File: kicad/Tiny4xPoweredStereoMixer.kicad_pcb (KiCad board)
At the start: 4 copper layers, 84 x 67.2 mm, 62 parts, among them J1 AudioJack3_SwitchTR, J2 AudioJack3_SwitchTR, J3 AudioJack3_SwitchTR, J4 AudioJack3_SwitchTR, J5 PowerConnector, J9 AudioJack3_SwitchTR, U1 TL072, U2 TL072, U3 TPS54202DDC

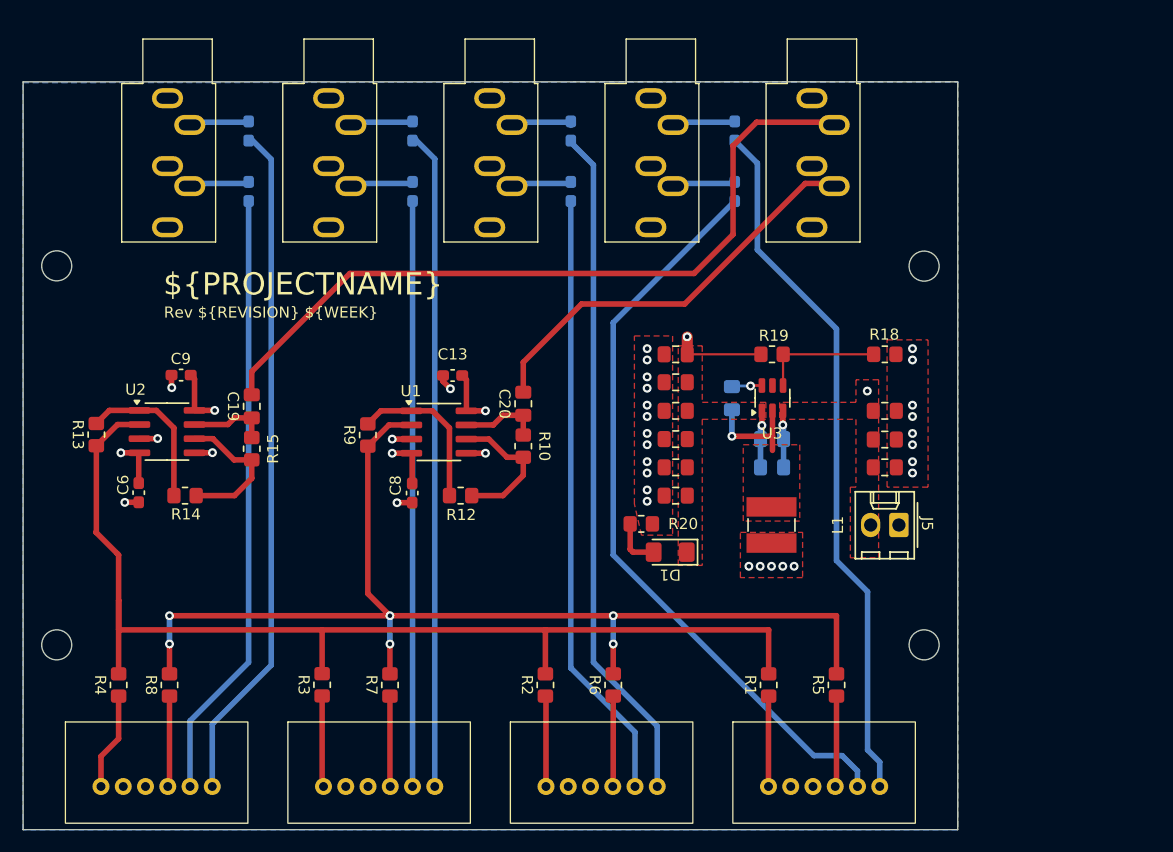
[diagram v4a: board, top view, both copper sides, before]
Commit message: PSU now uses +/- 2.5V; Added barrel jack; updated layout
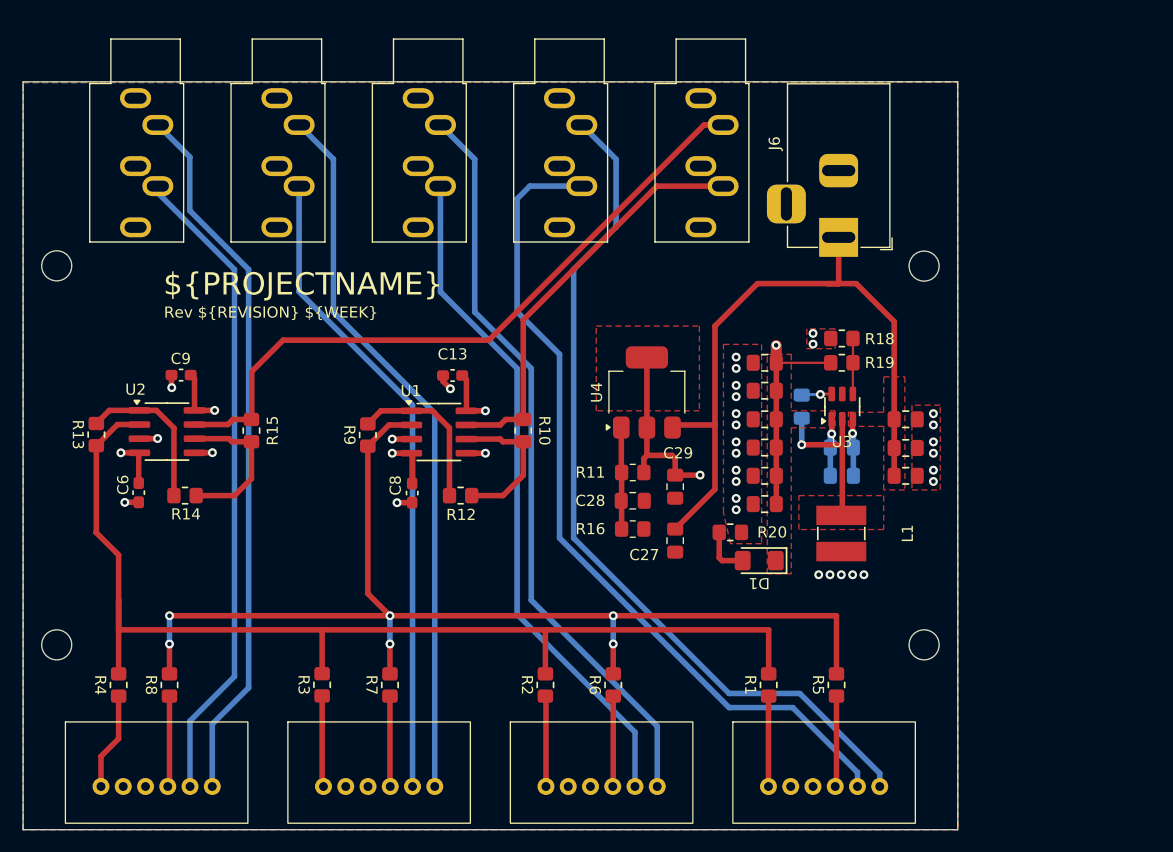
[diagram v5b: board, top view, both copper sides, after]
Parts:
- removed C10, C11, C12, C14, C17, C18, C5, C7: 100nF, Capacitor_SMD:C_0603_1608Metric_Pad1.08x0.95mm_HandSolder
- removed C19, C20: 10uF, Capacitor_SMD:C_0805_2012Metric_Pad1.18x1.45mm_HandSolder
- removed J5: PowerConnector, Connector_Molex:Molex_KK-254_AE-6410-02A_1x02_P2.54mm_Vertical
- added C27: 10uF, Capacitor_SMD:C_0805_2012Metric_Pad1.18x1.45mm_HandSolder, F.Cu at (160.3, 91.7)
- added C28: 22uF, Capacitor_SMD:C_0805_2012Metric_Pad1.18x1.45mm_HandSolder, F.Cu at (156.4, 88.1)
- added C29: 10uF, Capacitor_SMD:C_0805_2012Metric_Pad1.18x1.45mm_HandSolder, F.Cu at (160.3, 86.8)
- added J6: Barrel_Jack_Switch, Connector_BarrelJack:BarrelJack_Horizontal, F.Cu at (174.9, 64.4)
- added R11: 120R, Resistor_SMD:R_0805_2012Metric_Pad1.20x1.40mm_HandSolder, F.Cu at (156.4, 85.6)
- added R16: 120R, Resistor_SMD:R_0805_2012Metric_Pad1.20x1.40mm_HandSolder, F.Cu at (156.4, 90.6)
- added U4: LM1117MP-ADJ, Package_TO_SOT_SMD:SOT-223-3_TabPin2, F.Cu at (157.7, 78.4)
- moved J9 9.98 mm to (162.6, 51.9)
- moved J4 8.21 mm to (149.9, 51.9)
- moved C21 8.04 mm to (168.3, 85.9)
- moved C22 8.04 mm to (168.3, 88.4)
- moved C23 8.04 mm to (168.3, 75.7)
- moved C24 8.04 mm to (168.3, 78.2)
- moved C25 8.04 mm to (168.3, 80.8)
- moved C26 8.04 mm to (168.3, 83.3)
- moved D1 8.04 mm to (167.8, 93.5)
- moved R20 8.04 mm to (165.2, 90.9)
- moved J3 6.43 mm to (137.2, 51.9)
- moved C15 6.32 mm to (175.2, 83.3)
- moved C4 6.32 mm to (175.2, 85.9)
- moved R19 6.32 mm to (175.2, 75.7)
- moved C16 6.32 mm to (171.6, 79.6)
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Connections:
- net -12V renamed -2V5
- C1 pad 1: +12V -> +5V
- C13 pad 1: +12V -> +2V5
- C15 pad 1: +12V -> +5V
- C2 pad 1: +12V -> +5V
- C3 pad 1: +12V -> +5V
- C4 pad 1: +12V -> +5V
- C9 pad 1: +12V -> +2V5
- J1 pad R: Net-(C7-Pad1) -> Net-(J1-PadR)
- J1 pad T: Net-(C5-Pad1) -> Net-(J1-PadT)
- J2 pad R: Net-(C11-Pad1) -> Net-(J2-PadR)
- J2 pad T: Net-(C10-Pad1) -> Net-(J2-PadT)
- J3 pad R: Net-(C14-Pad1) -> Net-(J3-PadR)
- J3 pad T: Net-(C12-Pad1) -> Net-(J3-PadT)
- J4 pad R: Net-(C18-Pad1) -> Net-(J4-PadR)
- J4 pad T: Net-(C17-Pad1) -> Net-(J4-PadT)
- J9 pad R: Net-(C20-Pad2) -> Net-(J9-PadR)
- J9 pad T: Net-(C19-Pad2) -> Net-(J9-PadT)
- R10 pad 2: Net-(C20-Pad1) -> Net-(J9-PadR)
- R15 pad 2: Net-(C19-Pad1) -> Net-(J9-PadT)
- RV1 pad 3: Net-(C7-Pad2) -> Net-(J1-PadR)
- RV1 pad 6: Net-(C5-Pad2) -> Net-(J1-PadT)
- RV2 pad 3: Net-(C11-Pad2) -> Net-(J2-PadR)
- RV2 pad 6: Net-(C10-Pad2) -> Net-(J2-PadT)
- RV3 pad 3: Net-(C14-Pad2) -> Net-(J3-PadR)
- RV3 pad 6: Net-(C12-Pad2) -> Net-(J3-PadT)
- RV4 pad 3: Net-(C18-Pad2) -> Net-(J4-PadR)
- RV4 pad 6: Net-(C17-Pad2) -> Net-(J4-PadT)
- U1 pad 7: Net-(C20-Pad1) -> Net-(J9-PadR)
- U1 pad 8: +12V -> +2V5
- U2 pad 7: Net-(C19-Pad1) -> Net-(J9-PadT)
- U2 pad 8: +12V -> +2V5
- U3 pad 3: +12V -> +5V
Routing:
- net Net-(J4-PadT): track 0.00 -> 77.8 mm
- net Net-(J4-PadR): track 0.00 -> 75.5 mm
- net Net-(C19-Pad2): track 68.4 -> 0.00 mm
- net Net-(C18-Pad2): track 68.1 -> 0.00 mm
- net Net-(J3-PadT): track 0.00 -> 67.9 mm
- net +5V: track 0.00 -> 66.7 mm, vias 0 -> 1
- net Net-(J2-PadT): track 0.00 -> 64.9 mm
- net Net-(J1-PadT): track 0.00 -> 64.5 mm
- net Net-(C17-Pad2): track 63.8 -> 0.00 mm
- net Net-(C5-Pad2): track 61.6 -> 0.00 mm
- net Net-(C12-Pad2): track 61.6 -> 0.00 mm
- net Net-(J3-PadR): track 0.00 -> 61.5 mm
- net Net-(J9-PadT): track 0.00 -> 61.2 mm
- net Net-(C10-Pad2): track 59.4 -> 0.00 mm
- net Net-(J1-PadR): track 0.00 -> 58.8 mm
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- added copper zone on F.Cu, net +2V5
- added copper zone on In1.Cu, net +2V5
- added copper zone on F.Cu, net +5V
- added copper zone on In1.Cu, net +5V
- removed copper zone on F.Cu, net +12V
- removed copper zone on In1.Cu, net +12V
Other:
- board text added: "Enclosure: https://www.hammfg.com/files/parts/pdf/RM2005M.pdf"
- board text removed: "Enclosure: https://www.hammfg.com/files/parts/pdf/RM2005S.pdf"

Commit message: Created missing SOT-23-THIN-14 footprint; Replaced 2xTL072 with 1xTL074; updated layout
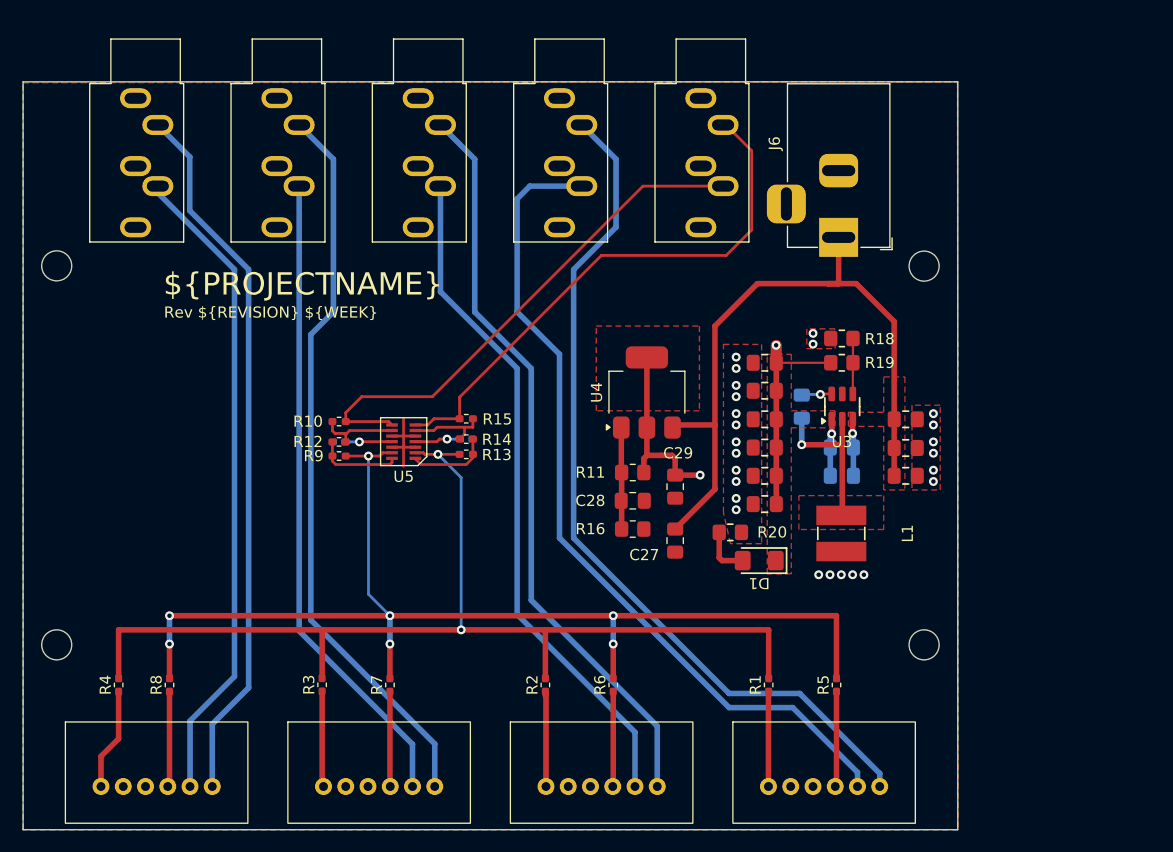
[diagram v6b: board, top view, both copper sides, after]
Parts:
- removed C13, C6: 100nF, Capacitor_SMD:C_0603_1608Metric_Pad1.08x0.95mm_HandSolder
- removed U1, U2: TL072, Package_SO:SOIC-8_3.9x4.9mm_P1.27mm
- added U5: TL074, SOT-23-THIN-14:SOIC-14, F.Cu at (135.9, 82.8)
- C8, C9: footprint Capacitor_SMD:C_0603_1608Metric_Pad1.08x0.95mm_HandSolder -> Capacitor_SMD:C_0402_1005Metric_Pad0.74x0.62mm_HandSolder; moved to B.Cu
- R1, R10, R12, R13, R14, R15, R2, R3, R4, R5, R6, R7, R8, R9: footprint Resistor_SMD:R_0805_2012Metric_Pad1.20x1.40mm_HandSolder -> Resistor_SMD:R_0402_1005Metric_Pad0.72x0.64mm_HandSolder
- moved R13 33.3 mm to (141.5, 83.9), turned to 0 degrees
- moved C9 26.3 mm to (141.5, 82.5), turned to 0 degrees
- moved R14 25.8 mm to (141.5, 82.5), turned to 180 degrees
- moved R15 19.3 mm to (141.5, 80.7), turned to 180 degrees
- moved R10 16.6 mm to (130.0, 81.0), turned to 0 degrees
- moved R12 11.9 mm to (130.0, 82.8)
- moved C8 8.02 mm to (130.0, 82.8), turned to 180 degrees
- moved R9 3.20 mm to (130.0, 84.1), turned to 180 degrees
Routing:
- net Net-(J9-PadT): track 61.2 -> 49.3 mm
- net Net-(J9-PadR): track 37.2 -> 47.4 mm
- net Net-(R13-Pad2): track 14.2 -> 7.11 mm
- net Net-(U5B--): track 14.1 -> 7.30 mm
- net Net-(R12-Pad1): track 14.5 -> 7.79 mm
- net Net-(U5C--): track 13.6 -> 7.19 mm
- net +2V5: track 27.1 -> 21.0 mm, vias 3 -> 2
- net -2V5: track 33.2 -> 28.5 mm, vias 4 -> 3
- net GND: track 11.9 -> 8.47 mm, vias 33 -> 25
- net Net-(U5A--): track 98.9 -> 96.5 mm, vias 0 -> 2
- net Net-(J2-PadT): track 64.9 -> 66.5 mm
- net /ch4_left_mix_in: track 8.48 -> 9.29 mm
- net /ch3_left_mix_in: track 8.50 -> 9.30 mm
- net Net-(U5D--): track 101.6 -> 101.9 mm, vias 6 -> 7
